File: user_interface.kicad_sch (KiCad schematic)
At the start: 27 parts, among them J1201 Conn_01x08, J1202 36103505, J1203 5051104091, U1201 TCA9554PW, U1202 STLD40DPUR

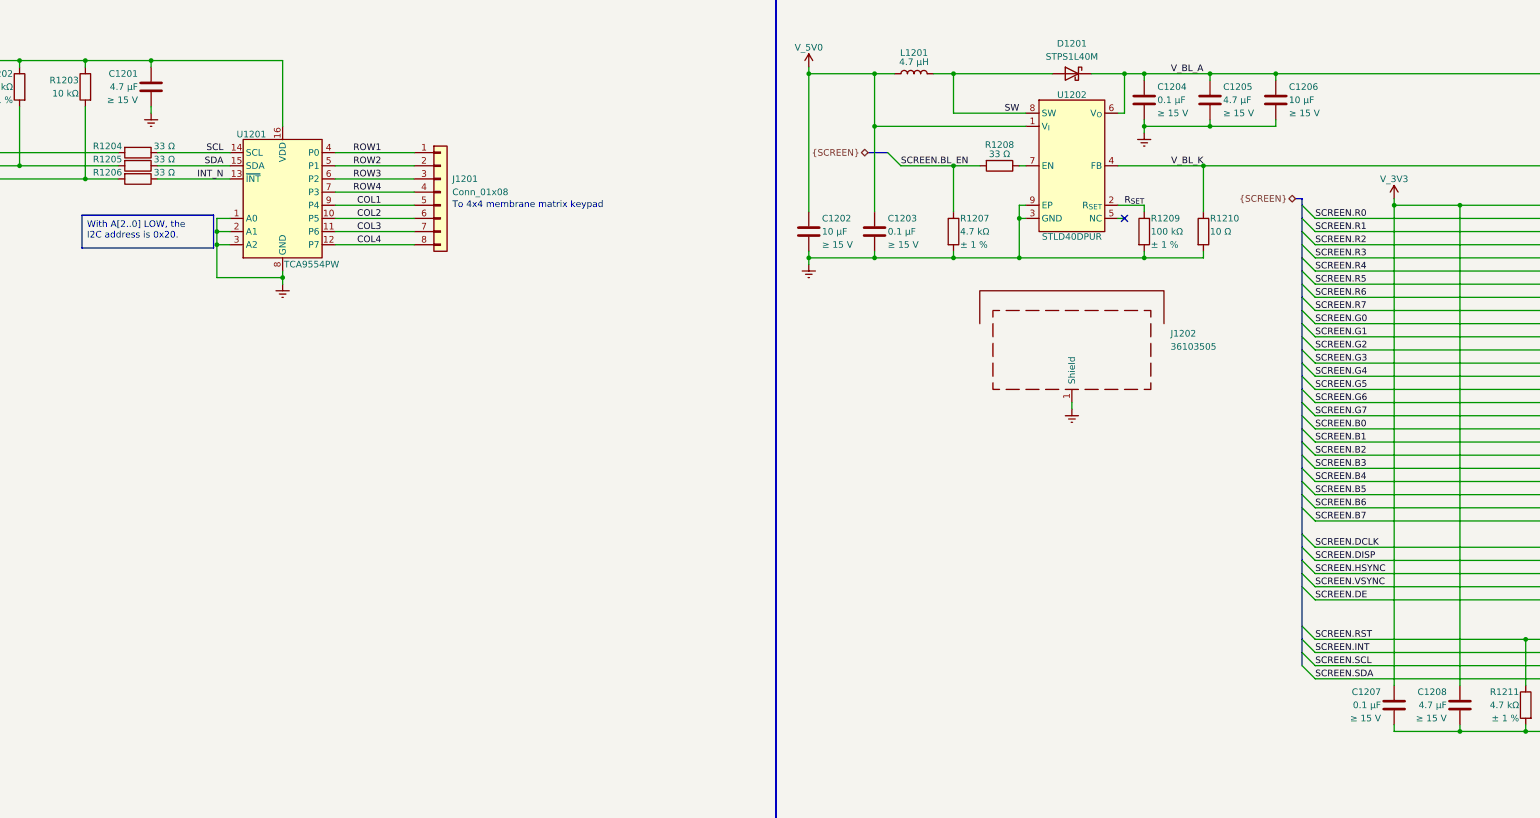
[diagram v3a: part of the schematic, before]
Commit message: Fix component values
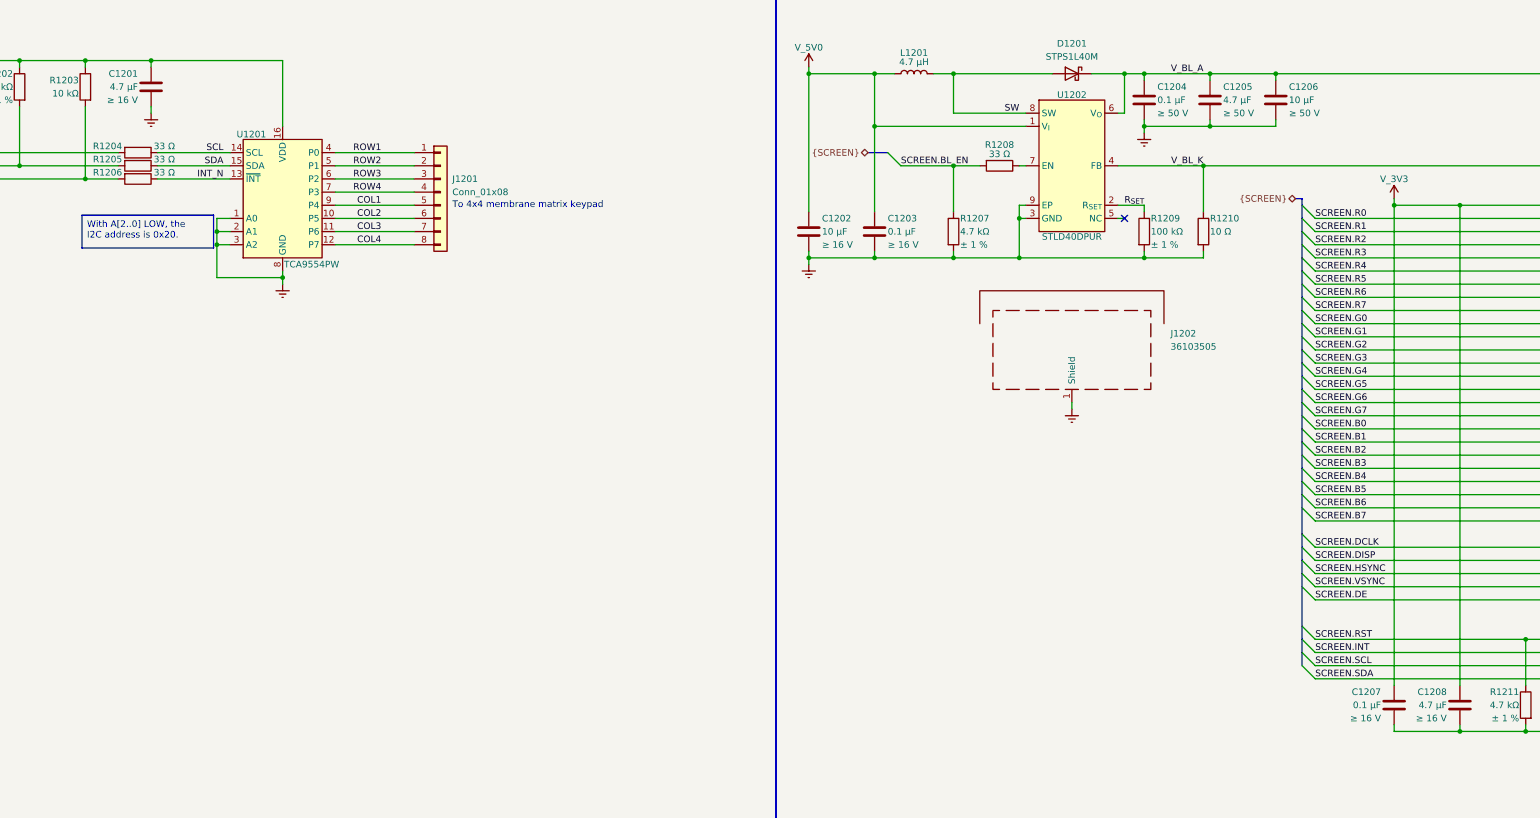
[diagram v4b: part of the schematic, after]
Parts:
- C1201, C1202, C1203, C1207, C1208: Voltage rating ≥ 15 V -> ≥ 16 V
- C1204, C1205, C1206: Voltage rating ≥ 15 V -> ≥ 50 V
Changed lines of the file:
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@@
 			)
 		)
-		(property "Voltage rating" "≥ 15 V"
+		(property "Voltage rating" "≥ 16 V"
 			(at 339.09 228.6001 0)
 			(effects
@@
 			)
 		)
-		(property "Voltage rating" "≥ 15 V"
+		(property "Voltage rating" "≥ 16 V"
 			(at 86.36 109.2201 0)
 			(effects
@@
 			)
 		)
-		(property "Voltage rating" "≥ 15 V"
+		(property "Voltage rating" "≥ 16 V"
 			(at 218.44 137.1601 0)
 			(effects
@@
 			)
 		)
-		(property "Voltage rating" "≥ 15 V"
+		(property "Voltage rating" "≥ 50 V"
 			(at 283.21 111.7601 0)
 			(effects
@@
 			)
 		)
-		(property "Voltage rating" "≥ 15 V"
+		(property "Voltage rating" "≥ 50 V"
 			(at 308.61 111.7601 0)
 			(effects
@@
 			)
 		)
-		(property "Voltage rating" "≥ 15 V"
+		(property "Voltage rating" "≥ 16 V"
 			(at 326.39 228.6001 0)
 			(effects
@@
 			)
 		)
-		(property "Voltage rating" "≥ 15 V"
+		(property "Voltage rating" "≥ 16 V"
 			(at 231.14 137.1601 0)
 			(effects
@@
 			)
 		)
-		(property "Voltage rating" "≥ 15 V"
+		(property "Voltage rating" "≥ 50 V"
 			(at 295.91 111.7601 0)
 			(effects

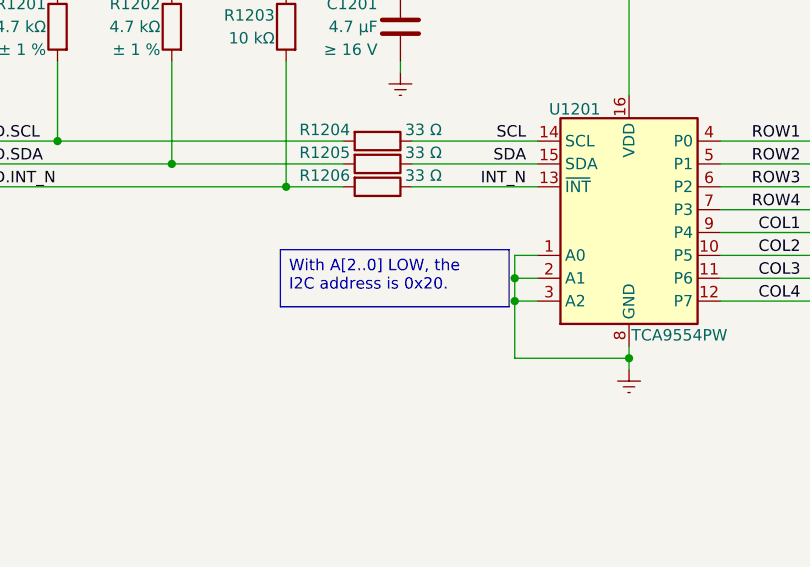
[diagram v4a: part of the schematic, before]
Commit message: Refactor schematics
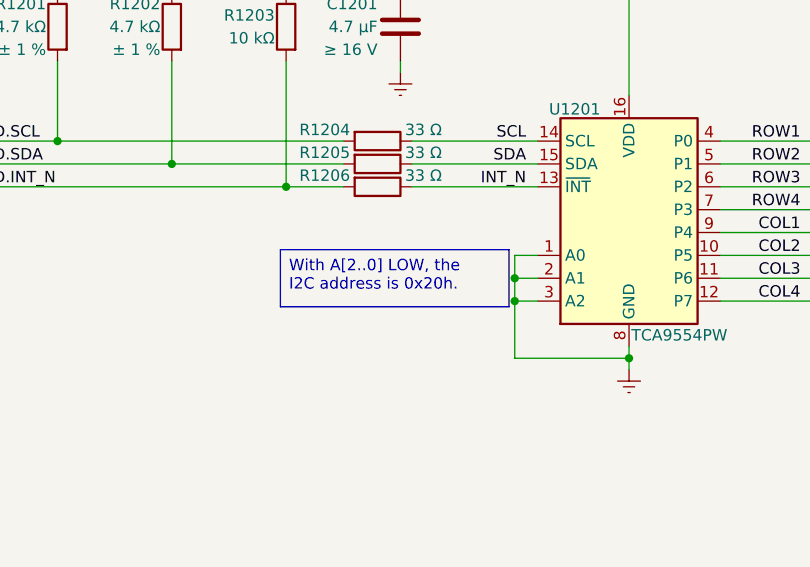
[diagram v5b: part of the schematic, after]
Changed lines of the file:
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@@
 		)
 	)
-	(text_box "With A[2..0] LOW, the I2C address is 0x20."
+	(text_box "With A[2..0] LOW, the I2C address is 0x20h."
 		(exclude_from_sim no)
 		(at 75.565 131.445 0)

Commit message: Clean-up schematics
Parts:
- R1204, R1205, R1206, R1208: value 33 Ω -> 0 Ω
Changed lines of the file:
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@@
 			)
 		)
-		(property "Value" "33 Ω"
+		(property "Value" "0 Ω"
 			(at 252.73 120.396 90)
 			(effects
@@
 			)
 		)
-		(property "Value" "33 Ω"
+		(property "Value" "0 Ω"
 			(at 89.408 123.952 90)
 			(effects
@@
 			)
 		)
-		(property "Value" "33 Ω"
+		(property "Value" "0 Ω"
 			(at 89.408 121.412 90)
 			(effects
@@
 			)
 		)
-		(property "Value" "33 Ω"
+		(property "Value" "0 Ω"
 			(at 89.408 118.872 90)
 			(effects

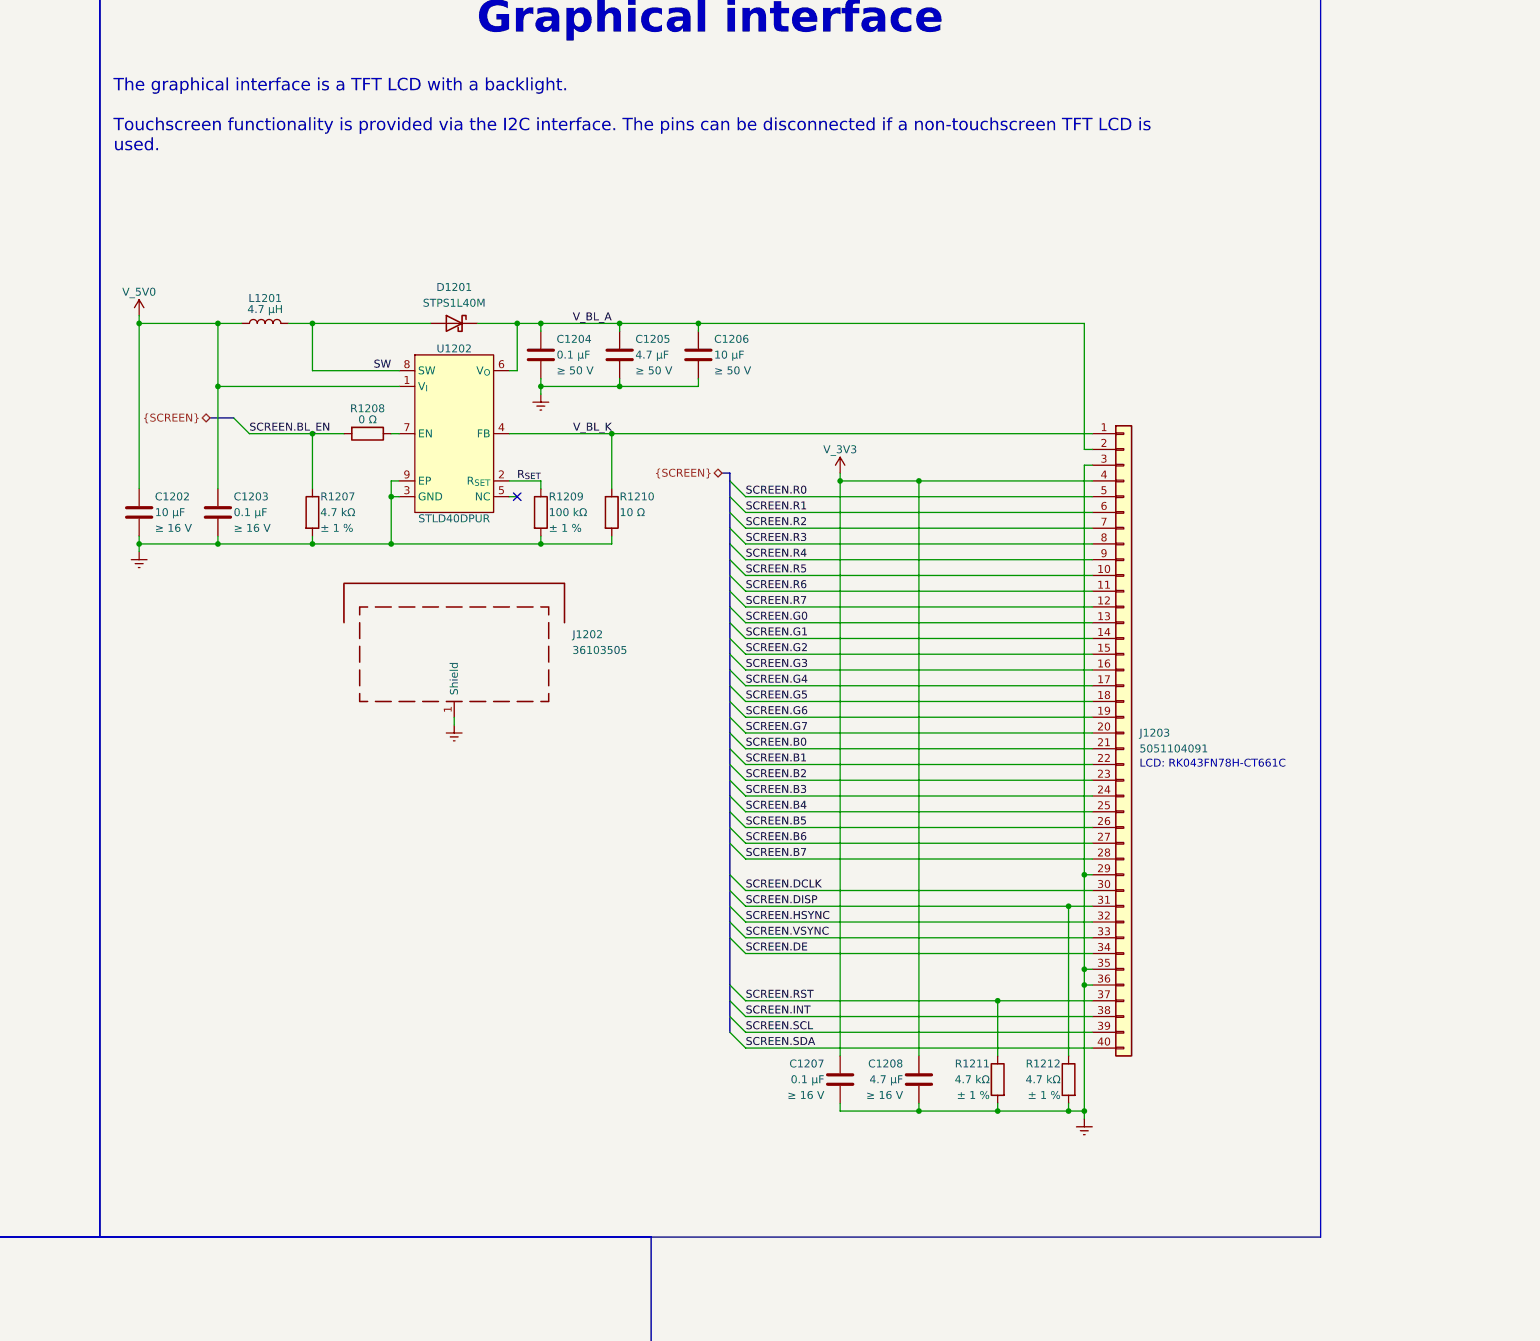
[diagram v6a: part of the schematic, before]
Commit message: Rework UI
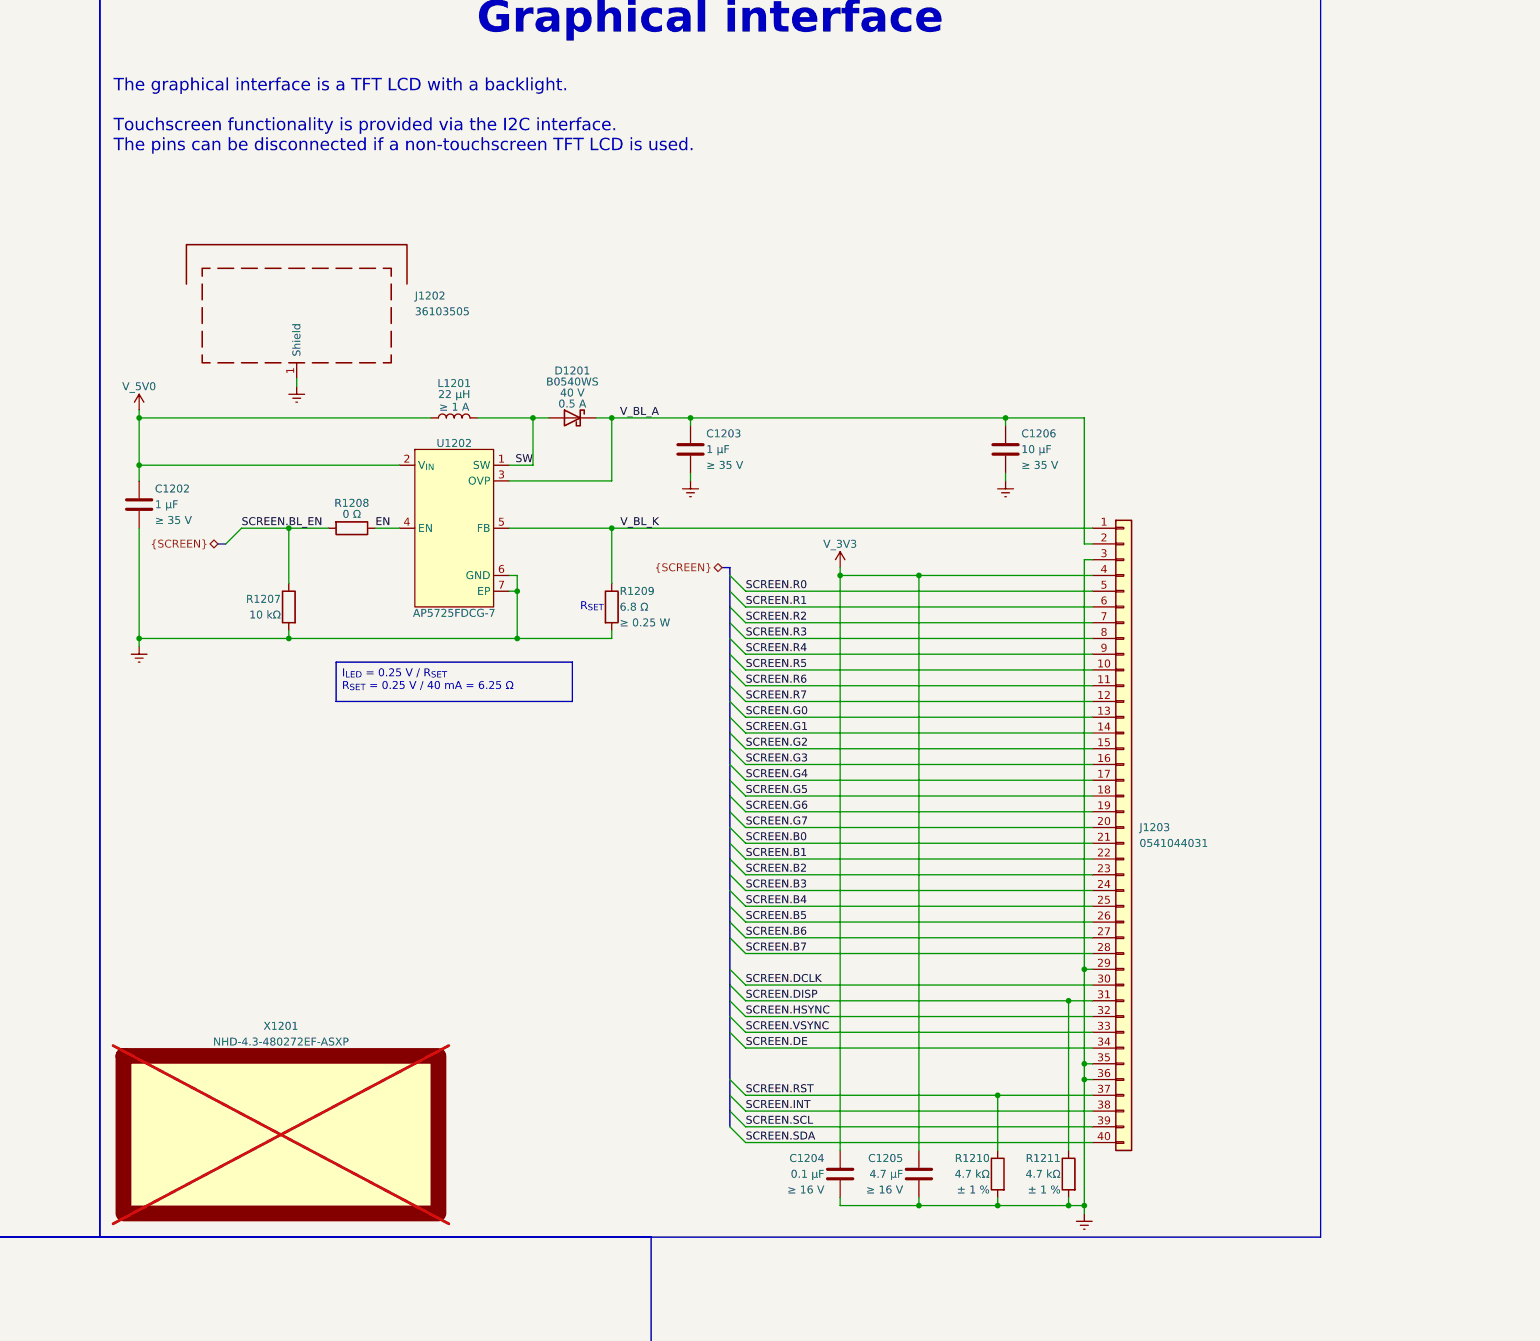
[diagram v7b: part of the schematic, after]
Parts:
- removed C1204: 0.1 µF, symbol Device:C
- removed C1205: 4.7 µF, Capacitor_SMD:C_0603_1608Metric, symbol Device:C
- removed R1209: 100 kΩ, perfect_footprints:R_0402_1005Metric, symbol Device:R
- removed U1202: STLD40DPUR, Package_DFN_QFN:DFN-8-1EP_3x3mm_P0.65mm_EP1.55x2.4mm, symbol STMicroelectronics:STLD40DPUR
- added U1202: AP5725FDCG-7, Package_DFN_QFN:DFN-6-1EP_2x2mm_P0.65mm_EP1.01x1.7mm, symbol Diodes Incorporated:AP5725FDCG-7
- added X1201: NHD-4.3-480272EF-ASXP, symbol linux-sbc:NHD-4.3-480272EF-ASXP
- C1202: value 10 µF -> 1 µF; Voltage rating ≥ 16 V -> ≥ 35 V
- C1203: value 0.1 µF -> 1 µF; Voltage rating ≥ 16 V -> ≥ 35 V
- C1206: footprint (none) -> Capacitor_SMD:C_0603_1608Metric; MPN (none) -> GRM188R6YA106MA73D; Manufacturer (none) -> Murata Electronics; Voltage rating ≥ 50 V -> ≥ 35 V
- D1201: value STPS1L40M -> B0540WS; footprint (none) -> Diode_SMD:D_SOD-323_HandSoldering; Current rating (none) -> 0.5 A; Digi-Key Part Number (none) -> 5399-B0540WSCT-ND; MPN (none) -> B0540WS; Manufacturer (none) -> Shenzhen Slkormicro Semicon Co., Ltd.; Voltage rating (none) -> 40 V
- J1203: value 5051104091 -> 0541044031
- L1201: value 4.7 µH -> 22 µH; footprint (none) -> Inductor_SMD:L_TechFuse_SL0630; Current rating (none) -> ≥ 1 A; Digi-Key Part Number (none) -> 283-HCM1A0703V3-220-RCT-ND; MPN (none) -> HCM1A0703V3-220-R; Manufacturer (none) -> Eaton - Electronics Division
- R1207: value 4.7 kΩ -> 10 kΩ; MPN (none) -> 560112110020; Manufacturer (none) -> Würth Elektronik; Tolerance ± 1 % -> (none)
- R1209: renamed from R1210; value 10 Ω -> 6.8 Ω; footprint perfect_footprints:R_0402_1005Metric -> Resistor_SMD:R_0805_2012Metric; Digi-Key Part Number (none) -> 541-6.80TCT-ND; MPN (none) -> CRCW08056R80FKEAHP; Manufacturer (none) -> Vishay Dale
- renumbered C1207 to C1204, C1208 to C1205, R1211 to R1210, R1212 to R1211
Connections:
- net GND: now also U1202.6 (GND), U1202.7 (EP)
- net SW: now also U1202.1 (SW)
- net V_5V0: now also U1202.2 (V_{IN}); no longer C1203.1
- net V_BL_A: now also C1203.1, U1202.3 (OVP)
- net V_BL_K: now also U1202.5 (FB)
- net EN: now reaches R1208.1
- net EN: now also U1202.4 (EN)
- no-connect marks 1 -> 0
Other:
- note added: "R_{SET}"
- note removed: "LCD: RK043FN78H-CT661C"
- moved on the sheet: C1204, C1205, D1201, J1202, J1203, L1201, R1208, R1209, R1210, R1211

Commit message: Add additional info to passives
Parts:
- C1201, C1205: footprint Capacitor_SMD:C_0603_1608Metric -> (none); MPN GRM188R6YA475KE15D -> (none); Manufacturer Murata Electronics -> (none); Size (none) -> 0603; Temperature coefficient (none) -> X5R; Tolerance (none) -> 20 %; Voltage rating ≥ 16 V -> 35 V
- C1202, C1203: Size (none) -> 0603; Temperature coefficient (none) -> X5R; Tolerance (none) -> 20 %; Voltage rating ≥ 35 V -> 35 V
- C1204: Size (none) -> 0402; Temperature coefficient (none) -> X5R; Tolerance (none) -> 20 %; Voltage rating ≥ 16 V -> 16 V
- C1206: footprint Capacitor_SMD:C_0603_1608Metric -> (none); MPN GRM188R6YA106MA73D -> (none); Manufacturer Murata Electronics -> (none); Size (none) -> 0805; Temperature coefficient (none) -> X5R; Tolerance (none) -> 20 %; Voltage rating ≥ 35 V -> 35 V
- R1201, R1202, R1210, R1211: Power rating (none) -> 0.1 W; Size (none) -> 0402; Tolerance ± 1 % -> 1 %
- R1203, R1207: MPN 560112110020 -> (none); Manufacturer Würth Elektronik -> (none); Power rating (none) -> 0.1 W; Size (none) -> 0402; Tolerance (none) -> 1 %
- R1204, R1205, R1206, R1208: footprint perfect_footprints:R_0402_1005Metric -> (none); MPN 560112110020 -> (none); Manufacturer Würth Elektronik -> (none); Size (none) -> 0402
- R1209: Digi-Key Part Number 541-6.80TCT-ND -> (none); MPN CRCW08056R80FKEAHP -> (none); Manufacturer Vishay Dale -> (none); Power rating ≥ 0.25 W -> 0.25 W; Size (none) -> 0805; Tolerance (none) -> 1 %
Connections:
- net EN: now also R1208.2; no longer R1208.1
- net INT_N: now also R1206.2; no longer R1206.1
- net KEYPAD.INT_N: now also R1206.1; no longer R1206.2
- net KEYPAD.SCL: now also R1204.1; no longer R1204.2
- net KEYPAD.SDA: now also R1205.1; no longer R1205.2
- net SCL: now also R1204.2; no longer R1204.1
- net SCREEN.BL_EN: now also R1208.1; no longer R1208.2
- net SDA: now also R1205.2; no longer R1205.1
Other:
- moved on the sheet: D1201, J1202, J1203, L1201, U1202, X1201
